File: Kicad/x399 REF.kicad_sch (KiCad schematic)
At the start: 57 parts, among them J1 +15V, J2 10Vref, Q1 MMBT3904, Q2 2SD882, U1 LM399, U2 OP07

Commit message: Add files via upload
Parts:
- D1, D4, D5: value STPS130 -> SS34A
- R9: value 220k -> Calc
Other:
- note added: "0603, 0.9 ohm"
- note added: "DCR=3.7R 12 mW"
- note added: "JP1, JP2 for parallel or series trim or TC comp"
- note added: "R9 TC/drift impact calculation R9 will have most impact when RV1 shunts it across R3 In that case R9 TC/drift is attenuated by R9/R3 For the 10mV example R9/R3 = 4545 kOhm/10.4 kOhm=437 Something like a 25ppm PTF is reasonable for R9"
- note added: "R9 calculation: Assume RV1 is a voltage source with Ro=0, for this R9>>RV1 Vin_{range}= (Vin_{max}-Vin_{min}) Where Vin_{range} - range of input voltage from RV1; Vin_{max} - the maximum input voltage from RV1 (10V); -Vin_{min} - minimum input voltage from RV1 (0V). Trim_{range}= (Vin_{range}/R9)*(R5||R6) R9 for a certain trim range= R9= (Vin_{range}/Trim_{range})*(R5||R6) For example for a desir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"
- note added: "RV1 TC/drift impact calculation RV1 ratio TC/drift is attenuated by Vin_{range}/Trim_{range} For the 10mV trim example Vin_{range}/Trim_{range}= 10V/10mV=1000 Wirewound pot for RV1"
- note removed: "DCR=6R 20 mW"
- note removed: "JP1, JP2 for trim or TC comp"
- moved on the sheet: C1, C10, C11, C12, C13, C2, C3, C4, C5, C6, C7, C8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

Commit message: Replace DIP8-400mil wide footprint to standard 300mil
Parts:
- U2: footprint Package_DIP:DIP-8_W7.62mm_PLUS SOIC -> Package_DIP:DIP-8_W7.62mm_W_soic_under
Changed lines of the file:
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@@
 			)
 		)
-		(property "Footprint" "Package_DIP:DIP-8_W7.62mm_PLUS SOIC"
+		(property "Footprint" "Package_DIP:DIP-8_W7.62mm_W_soic_under"
 			(at 204.47 54.61 0)
 			(effects
@@
 			)
 		)
-		(property "Footprint" "Package_DIP:DIP-8_W7.62mm_PLUS SOIC"
+		(property "Footprint" "Package_DIP:DIP-8_W7.62mm_W_soic_under"
 			(at 102.87 72.39 0)
 			(effects

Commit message: Add files via upload
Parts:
- added C14, C15, C16, C17, C18, C19: 100n, Capacitor_SMD:C_0805_2012Metric_Pad1.18x1.45mm_HandSolder, symbol Device:C
- added D6: 15V, Diode_SMD:D_SOD-323_HandSoldering, symbol Diode:BZX384xxxx
- added F2: 0ZCG0075BF2B, Resistor_SMD:R_0603_1608Metric_Pad0.98x0.95mm_HandSolder, symbol Device:Polyfuse
- added FL1: DR331-474BE, symbol Filter:Choke_CommonMode_FerriteCore_1423
- added L2: 20mH, symbol Device:Filter_EMI_CommonMode
- added Q3: AON7410, symbol Transistor_FET:Q_NMOS_GDS
- added R18, R19, R20, R21, R22: 1k, Resistor_SMD:R_0805_2012Metric_Pad1.20x1.40mm_HandSolder, symbol Device:R
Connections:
- net +10VREF: now also D6.1 (K), FL1.1, Q3.2 (D); no longer J2.1 (Pin_1)
- net Earth: now also C15.1, C18.1, C19.1, L2.1; no longer J1.2 (Pin_2)
- net MGND: now also FL1.2, Q3.3 (S), R22.1; no longer J2.2 (Pin_2)
- net at C3.1, D1.1 (K), D2.1 (K)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: now also C14.2, C16.2, C17.2, L2.3; no longer F1.2
- new net: C18.2, R20.2
- new net: C16.1, R18.1
- new net: C19.2, R21.2
- new net: D6.2 (A), Q3.1 (G), R22.2
- new net: F2.2, J2.1 (Pin_1)
- new net: FL1.3, J2.2 (Pin_2)
- new net: C17.1, R19.1
- new net: F1.2, L2.4
- new net: F2.1, FL1.4
- new net: J1.2 (Pin_2), L2.2
- new net guard: C14.1, C15.2, R18.2, R19.2, R20.1, R21.1
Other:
- note added: "0.26 ohm per leg"
- note added: "100n 250V X7R 1206 caps"
- note added: "1812, 0.11 ohms (typ)"
- note added: "DCR=3R per leg 24 mW"
- note added: "Q3, D5, F2 - thermally coupled"
- note removed: "10V star"
- moved on the sheet: C1, C10, C11, C12, C13, C2, C3, C4, C5, C6, C7, C8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

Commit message: Add files via upload
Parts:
- added R23, R24: 0R, symbol Device:R
- L2: value 20mH -> EE10 20mH
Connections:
- net +10VREF: now also R24.1
- net MGND: now also R23.1
- net at FL1.3, J2.2 (Pin_2): now also R23.2
- net at F2.1, FL1.4: now also R24.2
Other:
- note added: "1u cap = solid tantalum with >5 ohm ESR"
- note added: "R23, R24 are option to bypass output CMC, for better dc output resistance"
- note added: "TP6 is option to bypass output fuse for lower output resistance If bypassing fuse, consider DNP Q3, D5. Device will break with backfeed, but no risk of burnt pcb"
- note removed: "1u cap = solid tant/niob/alu with >5 ohm ESR"
- note removed: "R14 may be mounted on binding posts"
- note removed: "This is the MGND star MGND is star connected to the overall 0V input"
- moved on the sheet: C1, C10, C11, C12, C13, C14, C15, C16, C17, C18, C19, C2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

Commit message: Add files via upload
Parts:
- removed D1: SS34A, Diode_SMD:D_SMA_Handsoldering, symbol Device:D_Schottky
- removed L2: EE10 20mH, symbol Device:Filter_EMI_CommonMode
- removed R23, R24: 0R, symbol Device:R
- added FL2: 28mH, OwnStuff:Universal line filter, symbol Filter:Choke_CommonMode_FerriteCore_1423
- added J3: Guard, Connector_Wire:SolderWire-0.127sqmm_1x01_D0.48mm_OD1mm_Relief, symbol Connector_Generic:Conn_01x01
- added JP3, JP4, JP5: ~, TestPoint:TestPoint_2Pads_Pitch2.54mm_Drill0.8mm, symbol Jumper:Jumper_2_Open
- added R1alt: smd, Resistor_SMD:R_1206_3216Metric_Pad1.30x1.75mm_HandSolder, symbol Device:R
- C16, C17, C18, C19: value 100n -> 1u; footprint Capacitor_SMD:C_0805_2012Metric_Pad1.18x1.45mm_HandSolder -> Capacitor_SMD:C_1206_3216Metric_Pad1.33x1.80mm_HandSolder
- D6: value 15V -> BZX384B12
- F2: footprint Resistor_SMD:R_0603_1608Metric_Pad0.98x0.95mm_HandSolder -> Resistor_SMD:R_1812_4532Metric_Pad1.30x3.40mm_HandSolder
- FL1: footprint (none) -> OwnStuff:L_CommonMode_Bourns_DR331_Handsolder
- JP1, JP2: footprint Jumper:Joined holes D=1.8 Dh=0.9 P=3mm -> OwnStuff:Joined holes D=1.8 Dh=0.9 P=3mm
- L1: footprint Inductor_SMD:L_7.3x7.3_H4.5_Handsoldering -> OwnStuff:L_7.3x7.3_H4.5_Handsoldering
- Q3: footprint (none) -> OwnStuff:AO DFN3x3 EP GDS
- R13, R7: value 6R2 -> 6R8
- R18, R19, R20, R21: value 1k -> 470R
- R3, R5, R6: footprint Resistor_THT:S5-61 -> OwnStuff:S5-61+vishay(150mil)+smd1206
- RV1, RV2: footprint Potentiometer_THT:Potentiometer_Soviet_SP5-2VB -> OwnStuff:Potentiometer_Soviet_SP5-2VB
- TP2, TP3: footprint TestPoint:TestPoint_THTPad_D1.8mm_Drill0.9mm -> OwnStuff:TestPoint_THTPad_D1.8mm_Drill0.9mm
- U1: footprint Package_TO_SOT_THT:Analog_TO-46-4_ThermalShield_balanced pins -> OwnStuff:Analog_TO-46-4_ThermalShield_balanced pins
- U2: footprint Package_DIP:DIP-8_W7.62mm_W_soic_under -> OwnStuff:DIP-8_W7.62mm_W_soic_under
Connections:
- net +10VREF: now also F2.1, R1alt.2; no longer FL1.1
- net Earth: now also FL2.3; no longer H1.1
- net MGND: now also JP4.1 (A)
- net at R1.1, R2.2, TP1.1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: now also R1alt.1
- net at C5.1, C7.1, D4.1 (K)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: now also D2.1 (K)
- net at J2.1 (Pin_1): now also FL1.4, JP5.2 (B); no longer F2.2
- net at FL1.3, J2.2 (Pin_2): now also JP3.1 (A), JP4.2 (B)
- net at C14.2, C16.2, C17.2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: now also FL2.4; no longer D2.1 (K)
- net at F1.2: now also FL2.1
- net at J1.2 (Pin_2): now also FL2.2
- net guard renamed Guard
- net Guard: now also H1.1, J3.1 (Pin_1), JP3.2 (B)
- new net: F2.2, FL1.1, JP5.1 (A)
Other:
- note added: "0.26 (max) ohm per leg"
- note added: "1 ohm (max) total output resistance"
- note added: "100V 1206 X7R caps"
- note added: "JP5, JP4 are option to bypass output CMC, for better dc output resistance"
- note added: "RV1 TC/drift impact calculation Assuming RV1=0 ohms RV1 ratio TC/drift is attenuated by Vin_{range}/Trim_{range} For the 10mV trim example Vin_{range}/Trim_{range}= 10V/10mV=1000 Wirewound pot for RV1"
- note added: "TP6, TP5 is option to bypass output fuse for lower output resistance If bypassing fuse, consider DNP Q3, D5. Device will break with backfeed, but no risk of burnt pcb"
- note removed: "0.26 ohm per leg"
- note removed: "0603, 0.9 ohm"
- note removed: "100mW for 1k 10mW for 10k"
- note removed: "100n 250V X7R 1206 caps"
- note removed: "DCR=3R per leg 24 mW"
- note removed: "R23, R24 are option to bypass output CMC, for better dc output resistance"
- note removed: "RV1 TC/drift impact calculation RV1 ratio TC/drift is attenuated by Vin_{range}/Trim_{range} For the 10mV trim example Vin_{range}/Trim_{range}= 10V/10mV=1000 Wirewound pot for RV1"
- note removed: "TP6 is option to bypass output fuse for lower output resistance If bypassing fuse, consider DNP Q3, D5. Device will break with backfeed, but no risk of burnt pcb"
- moved on the sheet: C1, C10, C11, C12, C13, C2, C3, C4, C5, C6, C7, C8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

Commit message: Add files via upload
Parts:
- added C20, C21: 100n, Capacitor_SMD:C_0805_2012Metric_Pad1.18x1.45mm_HandSolder, symbol Device:C
- added C22, C23: 1u, Capacitor_THT:C_Rect_L4.6mm_W5.5mm_P2.50mm_MKS02_FKP02, symbol Device:C
- added H4: d=3.7, OwnStuff:MountingHole_3.7mm_Pad_Via_6.7mm diameter, symbol Mechanical:MountingHole_Pad
- added R23, R24: 47R, Resistor_SMD:R_0805_2012Metric_Pad1.20x1.40mm_HandSolder, symbol Device:R
- C4: renamed from C16; footprint Capacitor_SMD:C_1206_3216Metric_Pad1.33x1.80mm_HandSolder -> Capacitor_SMD:C_0805_2012Metric_Pad1.18x1.45mm_HandSolder
- C5: renamed from C18; footprint Capacitor_SMD:C_1206_3216Metric_Pad1.33x1.80mm_HandSolder -> Capacitor_SMD:C_0805_2012Metric_Pad1.18x1.45mm_HandSolder
- C6: renamed from C17; footprint Capacitor_SMD:C_1206_3216Metric_Pad1.33x1.80mm_HandSolder -> Capacitor_SMD:C_0805_2012Metric_Pad1.18x1.45mm_HandSolder
- C7: renamed from C19; footprint Capacitor_SMD:C_1206_3216Metric_Pad1.33x1.80mm_HandSolder -> Capacitor_SMD:C_0805_2012Metric_Pad1.18x1.45mm_HandSolder
- H3: renamed from H1; footprint MountingHole:MountingHole_3.7mm_Pad_Via -> OwnStuff:MountingHole_3.7mm_Pad_Via_6.7mm diameter
- Q3: footprint OwnStuff:AO DFN3x3 EP GDS -> OwnStuff:AO DFN3x3 EP GDS Handsoldering
- renumbered C14 to C1, C4 to C10, C5 to C11, C6 to C12, C7 to C13, C8 to C14, C9 to C15, C10 to C16, C12 to C17, C13 to C18, C11 to C19, C15 to C2, C1 to C3, C3 to C8, C2 to C9, D2 to D1, D3 to D2, D4 to D3, D6 to D4, FL2 to FL1, FL1 to FL2, H2 to H1, H3 to H2, J3 to J2, J2 to J3, JP5 to JP3, JP3 to JP5, R18 to R1, R5 to R10, R6 to R11, R8 to R12, R9 to R13, R10 to R14, R11 to R15, R12 to R16, R13 to R17, R14 to R18, R22 to R19, R1alt to R1alt1, R20 to R2, R15 to R20, R16 to R21, R17 to R22, R19 to R3, R21 to R4, R1 to R5, R2 to R6, R3 to R7, R7 to R8, R4 to R9, TP6 to TP5, TP5 to TP6
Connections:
- net MGND: now also FL2.1, C21.1, R24.2; no longer FL2.2
- net at J3.2 (Pin_2), JP4.2 (B), JP5.1 (A): now also FL2.4; no longer FL2.3
- net at J3.1 (Pin_1), JP3.2 (B): now also FL2.3; no longer FL2.4
- net at F2.2, JP3.1 (A): now also FL2.2, C20.2, R23.1; no longer FL2.1
- net Guard renamed Guard1
- net Guard1: no longer J2.1 (Pin_1), JP5.2 (B)
- new net: C22.2, R23.2
- new net: C23.1, R24.1
- new net Guard2: C20.1, C21.2, C22.1, C23.2, H4.1, J2.1 (Pin_1), JP5.2 (B)
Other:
- note added: "50V X7R caps"
- note added: "Guard1 and Guard2 connected via aluminum case"
- note added: "JP5, JP4 are option to bypass output CMC, for better dc output resistance Or when guard is tied to output ground for lower bom cost"
- note removed: "100V 1206 X7R caps"
- note removed: "1u cap = solid tantalum with >5 ohm ESR"
- note removed: "JP5, JP4 are option to bypass output CMC, for better dc output resistance"
- moved on the sheet: C1, C10, C11, C12, C13, C14, C15, C16, C17, C18, C19, C2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

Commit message: Add files via upload
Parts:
- added F1alt1: RXEF010, OwnStuff:RXEF010, symbol Device:Polyfuse
- added R13alt1: 0.6W tht, Resistor_THT:R_Axial_DIN0309_L9.0mm_D3.2mm_P12.70mm_Horizontal, symbol Device:R
- added R13alt2: 1206 smd, Resistor_SMD:R_1206_3216Metric_Pad1.30x1.75mm_HandSolder, symbol Device:R
- added R25: 0R, Resistor_SMD:R_0805_2012Metric_Pad1.20x1.40mm_HandSolder, symbol Device:R
- C18: value 100n NP0 -> 100n
- renumbered H3 to H1, H1 to H2, H2 to H3, R1alt1 to R5alt1
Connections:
- net +10VREF: now also R25.2; no longer C3.1
- net at R10.1, R11.1, R13.1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: now also R13alt1.1, R13alt2.1
- net at R13.2, RV1.2: now also R13alt1.2, R13alt2.2
- net at F1.1, J1.1 (Pin_1): now also F1alt1.1
- net at F1.2, FL1.1: now also F1alt1.2
- new net: C3.1, R25.1
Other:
- note added: "Q2 glued to metal enclosure via alumina or mica isolator"
- moved on the sheet: C3, D3

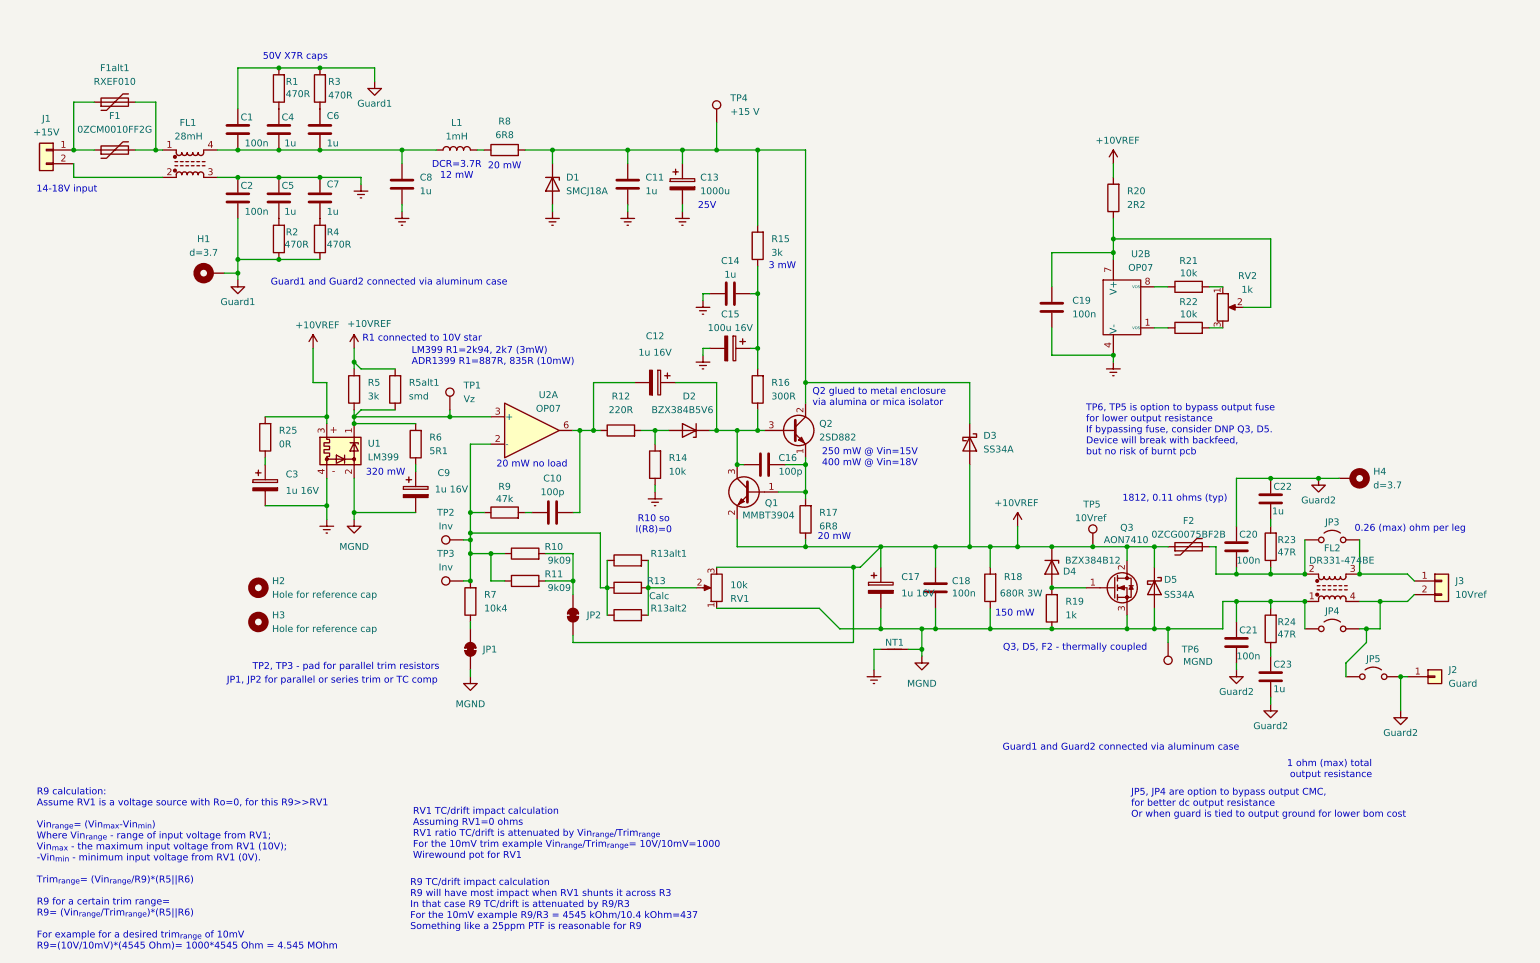
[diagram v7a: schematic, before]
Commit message: Add files via upload
Replaced guard2 1u film capacitors for more accessible ones, improved thermal design on output
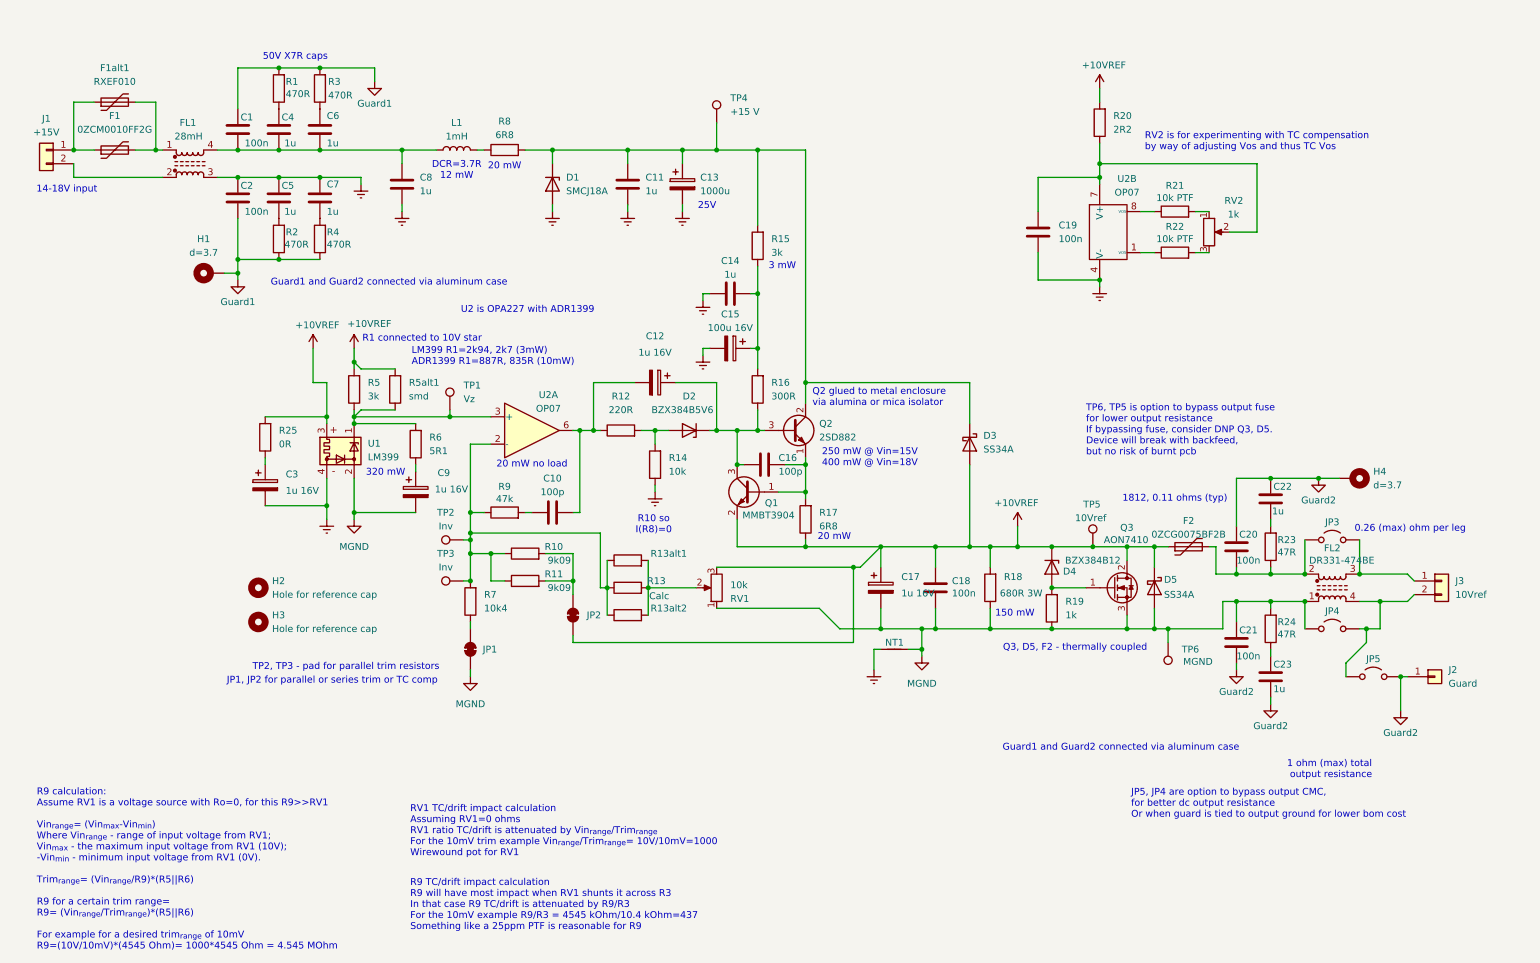
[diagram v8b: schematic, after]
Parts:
- C20, C21: footprint Capacitor_SMD:C_0805_2012Metric_Pad1.18x1.45mm_HandSolder -> Capacitor_SMD:C_1206_3216Metric_Pad1.33x1.80mm_HandSolder
- C22, C23: footprint Capacitor_THT:C_Rect_L4.6mm_W5.5mm_P2.50mm_MKS02_FKP02 -> OwnStuff:C_Rect_L7.2mm_W5mm_P5.00mm_FKS2_FKP2_MKS2_MKP2
- R21, R22: value 10k -> 10k PTF
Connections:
- net +10VREF: now also R18.1; no longer R18.2
- net MGND: now also R18.2; no longer R18.1
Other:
- note added: "RV2 is for experimenting with TC compensation by way of adjusting Vos and thus TC Vos"
- note added: "U2 is OPA227 with ADR1399"
- moved on the sheet: C19, R20, R21, R22, RV2, U2B
